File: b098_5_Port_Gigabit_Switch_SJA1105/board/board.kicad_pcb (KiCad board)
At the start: 2 copper layers, 8 x 3.1 mm, 25 parts, among them J1 DebugEdge_02x05, J2 002_SPI, U1 SJA1105ELY

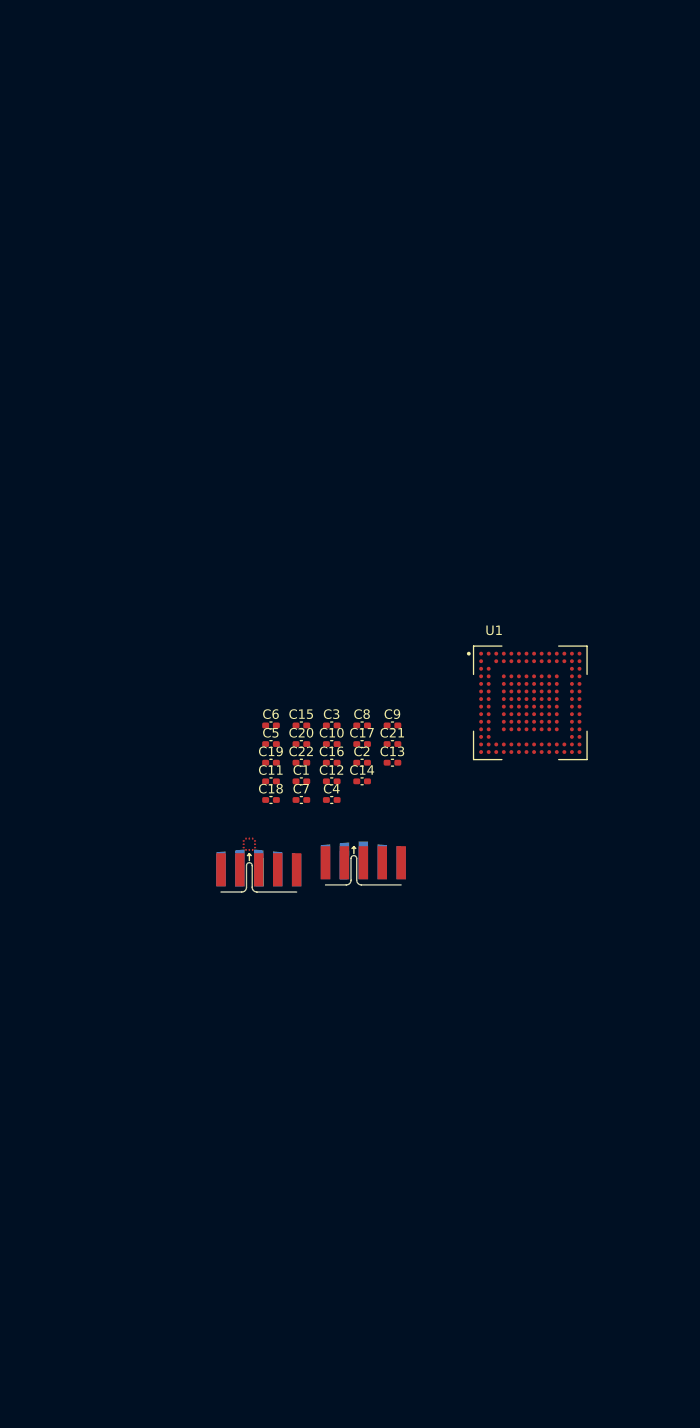
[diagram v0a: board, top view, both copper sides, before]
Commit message: added the rest of the MII interfaces
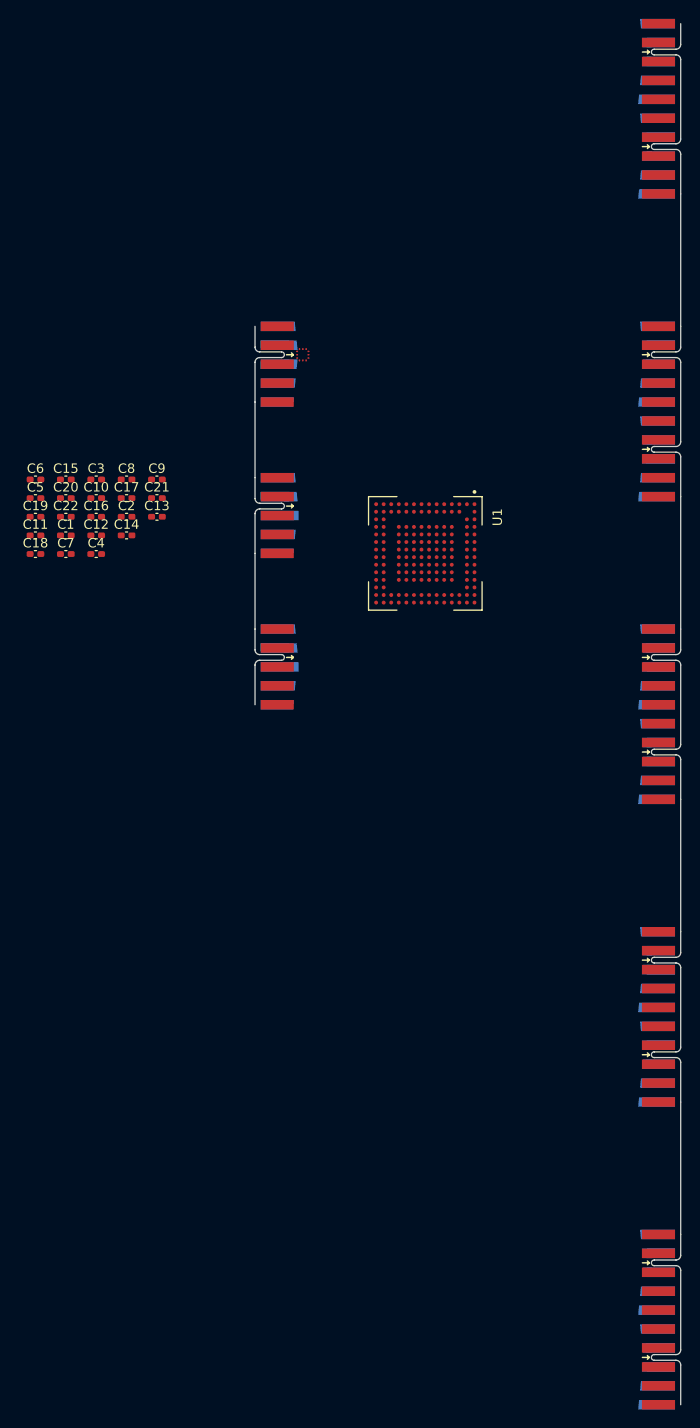
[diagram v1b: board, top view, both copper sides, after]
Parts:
- added J3: 015_RGMII, on_edge:on_edge_2x10_host, F.Cu at (160.0, 27.0)
- added J4: 015_RGMII, on_edge:on_edge_2x10_host, F.Cu at (160.0, 59.0)
- added J5: 015_RGMII, on_edge:on_edge_2x10_host, F.Cu at (160.0, 91.0)
- added J6: 015_RGMII, on_edge:on_edge_2x10_host, F.Cu at (160.0, 123.0)
- added J7: 015_RGMII, on_edge:on_edge_2x10_host, F.Cu at (160.0, 155.0)
- added J8: 003_power, on_edge:on_edge_2x05_device, F.Cu at (115.0, 91.0)
- moved J1 55.8 mm to (115.0, 59.0), turned to -90 degrees
- moved J2 40.7 mm to (115.0, 75.0), turned to -90 degrees
- moved C1 36.0 mm to (95.0, 77.1)
- moved C10 36.0 mm to (98.2, 73.2)
- moved C12 36.0 mm to (98.2, 77.1)
- moved C13 36.0 mm to (104.6, 75.1)
- moved C15 36.0 mm to (95.0, 71.2)
- moved C16 36.0 mm to (98.2, 75.1)
- moved C20 36.0 mm to (95.0, 73.2)
- moved C21 36.0 mm to (104.6, 73.2)
- moved C22 36.0 mm to (95.0, 75.1)
- moved C3 36.0 mm to (98.2, 71.2)
- moved C4 36.0 mm to (98.2, 79.1)
- moved C7 36.0 mm to (95.0, 79.1)
- moved C9 36.0 mm to (104.6, 71.2)
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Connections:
- net Net-(U1-PadD10) renamed /switch/VDDIO_MII2
- net Net-(U1-PadD4) renamed /switch/VDDIO_MII0
- net Net-(U1-PadD5) renamed /switch/VDDIO_MII1
- net Net-(U1-PadG11) renamed /switch/VDDIO_MII3
- net Net-(U1-PadL10) renamed /switch/VDDIO_MII4
- U1 pad A10: unconnected-(U1-PadA10) -> /switch/MII1_TX_ER
- U1 pad A11: unconnected-(U1-PadA11) -> /switch/MII2_RX_CTL
- U1 pad A12: unconnected-(U1-PadA12) -> /switch/MII2_RXD2
- U1 pad A13: unconnected-(U1-PadA13) -> /switch/MII2_RXD0
- U1 pad A2: unconnected-(U1-PadA2) -> /switch/MII0_TXD0
- U1 pad A3: unconnected-(U1-PadA3) -> /switch/MII0_TX_ER
- U1 pad A4: unconnected-(U1-PadA4) -> /switch/MII1_RX_CTL
- U1 pad A5: unconnected-(U1-PadA5) -> /switch/MII1_RXD2
- U1 pad A6: unconnected-(U1-PadA6) -> /switch/MII1_RXD0
- U1 pad A7: unconnected-(U1-PadA7) -> /switch/MII1_TXC
- U1 pad A8: unconnected-(U1-PadA8) -> /switch/MII1_TXD3
- U1 pad A9: unconnected-(U1-PadA9) -> /switch/MII1_TXD1
- U1 pad B1: unconnected-(U1-PadB1) -> /switch/MII0_TXD1
- U1 pad B10: unconnected-(U1-PadB10) -> /switch/MII2_RX_ER
- U1 pad B11: unconnected-(U1-PadB11) -> /switch/MII2_RXD3
- U1 pad B12: unconnected-(U1-PadB12) -> /switch/MII2_RXD1
- U1 pad B14: unconnected-(U1-PadB14) -> /switch/MII2_RXC
- U1 pad B3: unconnected-(U1-PadB3) -> /switch/MII1_RX_ER
- U1 pad B4: unconnected-(U1-PadB4) -> /switch/MII1_RXD3
- U1 pad B5: unconnected-(U1-PadB5) -> /switch/MII1_RXD1
- U1 pad B6: unconnected-(U1-PadB6) -> /switch/MII1_RXC
- U1 pad B7: unconnected-(U1-PadB7) -> /switch/MII1_TX_CTL
- U1 pad B8: unconnected-(U1-PadB8) -> /switch/MII1_TXD2
- U1 pad B9: unconnected-(U1-PadB9) -> /switch/MII1_TXD0
- U1 pad C1: unconnected-(U1-PadC1) -> /switch/MII0_TXD3
- U1 pad C13: unconnected-(U1-PadC13) -> /switch/MII2_TX_CTL
- U1 pad C14: unconnected-(U1-PadC14) -> /switch/MII2_TXC
- U1 pad C2: unconnected-(U1-PadC2) -> /switch/MII0_TXD2
- U1 pad D1: unconnected-(U1-PadD1) -> /switch/MII0_TXC
- U1 pad D13: unconnected-(U1-PadD13) -> /switch/MII2_TXD2
- U1 pad D14: unconnected-(U1-PadD14) -> /switch/MII2_TXD3
- U1 pad D2: unconnected-(U1-PadD2) -> /switch/MII0_TX_CTL
- U1 pad E1: unconnected-(U1-PadE1) -> /switch/MII0_RXD0
- U1 pad E13: unconnected-(U1-PadE13) -> /switch/MII2_TXD0
- U1 pad E14: unconnected-(U1-PadE14) -> /switch/MII2_TXD1
- U1 pad E2: unconnected-(U1-PadE2) -> /switch/MII0_RXC
- U1 pad F1: unconnected-(U1-PadF1) -> /switch/MII0_RXD2
- U1 pad F13: unconnected-(U1-PadF13) -> /switch/MII3_RX_ER
- U1 pad F14: unconnected-(U1-PadF14) -> /switch/MII2_TX_ER
- U1 pad F2: unconnected-(U1-PadF2) -> /switch/MII0_RXD1
- U1 pad G1: unconnected-(U1-PadG1) -> /switch/MII0_RX_CTL
- U1 pad G13: unconnected-(U1-PadG13) -> /switch/MII3_RXD3
- U1 pad G14: unconnected-(U1-PadG14) -> /switch/MII3_RX_CTL
- U1 pad G2: unconnected-(U1-PadG2) -> /switch/MII0_RXD3
- U1 pad H13: unconnected-(U1-PadH13) -> /switch/MII3_RXD1
- U1 pad H14: unconnected-(U1-PadH14) -> /switch/MII3_RXD2
- U1 pad H2: unconnected-(U1-PadH2) -> /switch/MII0_RX_ER
- U1 pad J13: unconnected-(U1-PadJ13) -> /switch/MII3_RXC
- U1 pad J14: unconnected-(U1-PadJ14) -> /switch/MII3_RXD0
- U1 pad K13: unconnected-(U1-PadK13) -> /switch/MII3_TX_CTL
- U1 pad K14: unconnected-(U1-PadK14) -> /switch/MII3_TXC
- U1 pad L13: unconnected-(U1-PadL13) -> /switch/MII3_TXD2
- U1 pad L14: unconnected-(U1-PadL14) -> /switch/MII3_TXD3
- U1 pad M13: unconnected-(U1-PadM13) -> /switch/MII3_TXD0
- U1 pad M14: unconnected-(U1-PadM14) -> /switch/MII3_TXD1
- U1 pad N10: unconnected-(U1-PadN10) -> /switch/MII4_RXD0
- U1 pad N11: unconnected-(U1-PadN11) -> /switch/MII4_RXD2
- U1 pad N12: unconnected-(U1-PadN12) -> /switch/MII4_RX_CTL
- U1 pad N14: unconnected-(U1-PadN14) -> /switch/MII3_TX_ER
- U1 pad N7: unconnected-(U1-PadN7) -> /switch/MII4_TXD1
- U1 pad N8: unconnected-(U1-PadN8) -> /switch/MII4_TXD3
- U1 pad N9: unconnected-(U1-PadN9) -> /switch/MII4_TXC
- U1 pad P10: unconnected-(U1-PadP10) -> /switch/MII4_RXC
- U1 pad P11: unconnected-(U1-PadP11) -> /switch/MII4_RXD1
- U1 pad P12: unconnected-(U1-PadP12) -> /switch/MII4_RXD3
- U1 pad P13: unconnected-(U1-PadP13) -> /switch/MII4_RX_ER
- U1 pad P6: unconnected-(U1-PadP6) -> /switch/MII4_TX_ER
- U1 pad P7: unconnected-(U1-PadP7) -> /switch/MII4_TXD0
- U1 pad P8: unconnected-(U1-PadP8) -> /switch/MII4_TXD2
- U1 pad P9: unconnected-(U1-PadP9) -> /switch/MII4_TX_CTL
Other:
- board size 8 x 3.1 mm -> 45 x 110 mm
